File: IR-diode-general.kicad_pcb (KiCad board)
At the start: 2 copper layers, 80 x 20.5 mm, 39 parts, among them J1 BarrelJack_3167288, J2 USB4105-GF-A, U1 QFN10_MP2483DQ_MNP, U2 AP62301Z6-7, U3 SM02B-SRSS-TB-LF-SN, U4 SM02B-SRSS-TB-LF-SN

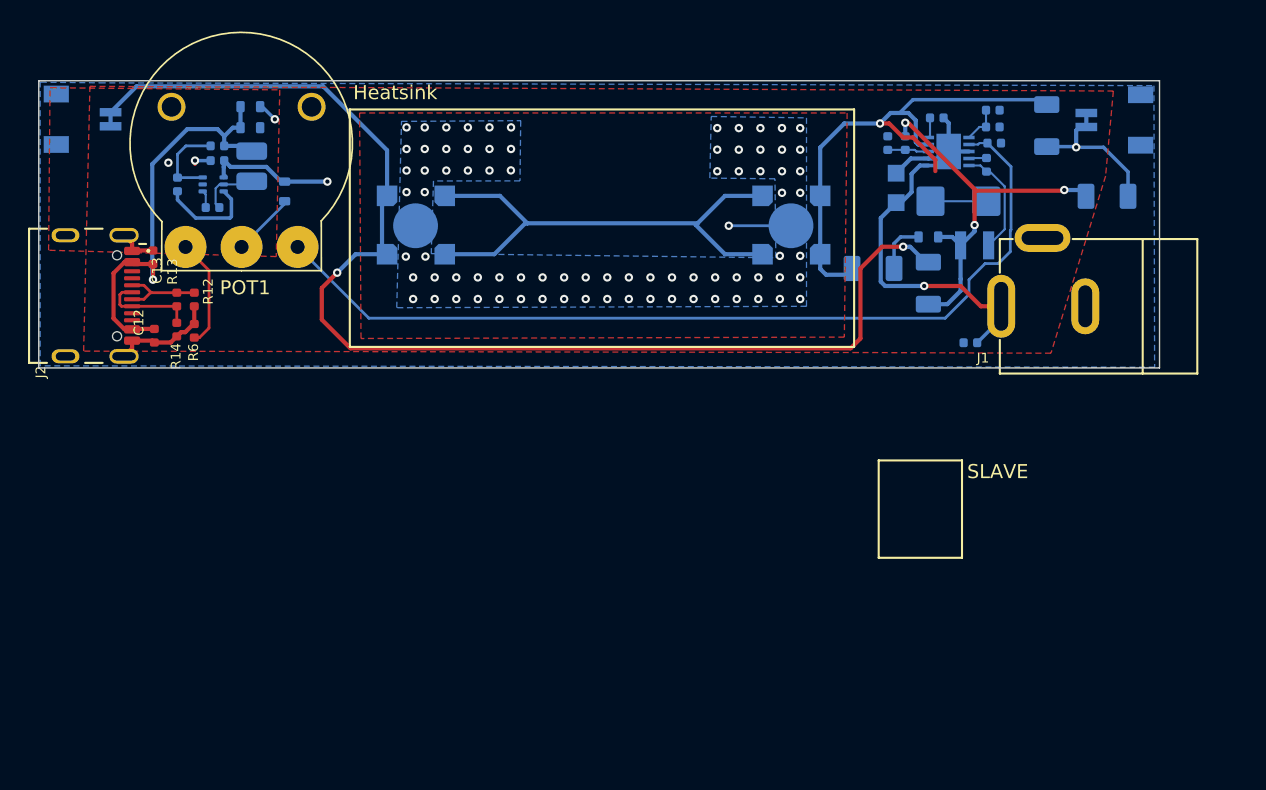
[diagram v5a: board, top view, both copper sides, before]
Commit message: Improving power rail tracks and planes
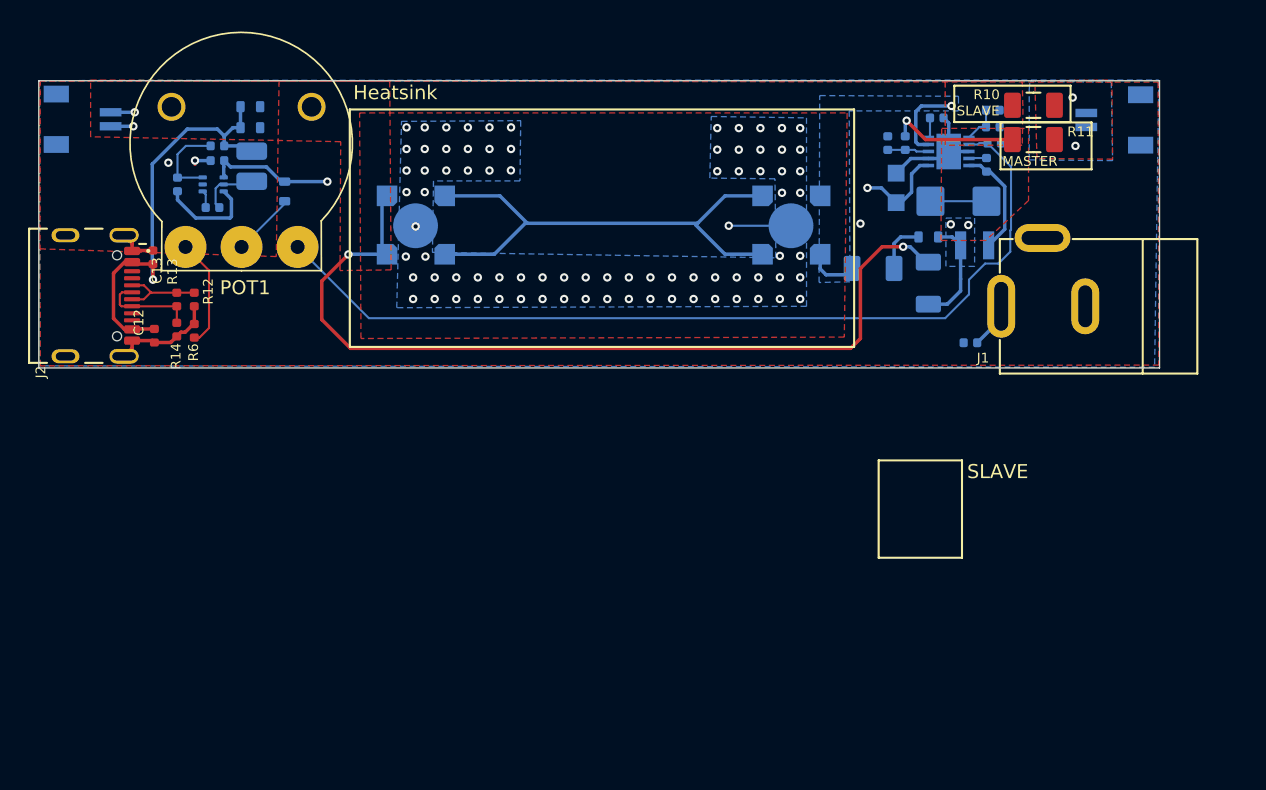
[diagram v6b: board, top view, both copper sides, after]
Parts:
- R10, R11: moved to F.Cu
- moved R11 6.63 mm to (156.0, 44.7)
- moved R10 1.73 mm to (156.0, 42.2), turned to 180 degrees
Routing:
- net FB: track 38.7 -> 9.55 mm
- net A_in: track 89.6 -> 66.6 mm, vias 2 -> 4
- net +12V: track 32.0 -> 19.1 mm
- net SW: track 28.3 -> 17.1 mm
- net C_out: track 11.3 -> 0.90 mm, vias 1 -> 2
- net GND: track 33.0 -> 31.7 mm
- net Thermal: vias 80 -> 81
- added copper zone on F.Cu, net A_in
- added copper zone on B.Cu, net C_out
- added copper zone on F.Cu, net C_out
- added copper zone on B.Cu, net FB
- added copper zone on F.Cu, net FB
- added copper zone on B.Cu, net SW
- added copper zone on F.Cu, net SW
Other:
- board text added: "DBG"

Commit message: Updated design rules
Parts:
- C6: value C_10p_0402 -> C_10u_25V_0603; footprint antmicro-footprints:C_0402_1005Metric -> antmicro-footprints:C_0603_1608Metric
- U1: value QFN10_MP2483DQ_MNP -> MP2483DQ-LF-P
- moved R8 0.55 mm to (97.8, 44.6)
- moved C6 0.43 mm to (97.4, 46.0), turned to 0 degrees
- moved C13 0.30 mm to (93.5, 53.0)
- moved POT1 0.27 mm to (99.6, 44.6)
- turned D1 to 180 degrees
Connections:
- C6 pad 1: +12V -> GND
- C6 pad 2: GND -> +12V
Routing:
- net (no net): track 4.00 -> 0.00 mm
- net FB: track 9.55 -> 5.87 mm
- net +12V: track 19.1 -> 17.0 mm
- net GND: track 31.7 -> 29.9 mm, vias 3 -> 2
- net Net-(C3-Pad1): track 7.86 -> 9.23 mm
- net A_in: track 66.6 -> 65.3 mm
- net /LED DRIVER & USB-C Power output/VBUS: track 31.2 -> 30.3 mm
- net C_out: track 0.90 -> 0.00 mm

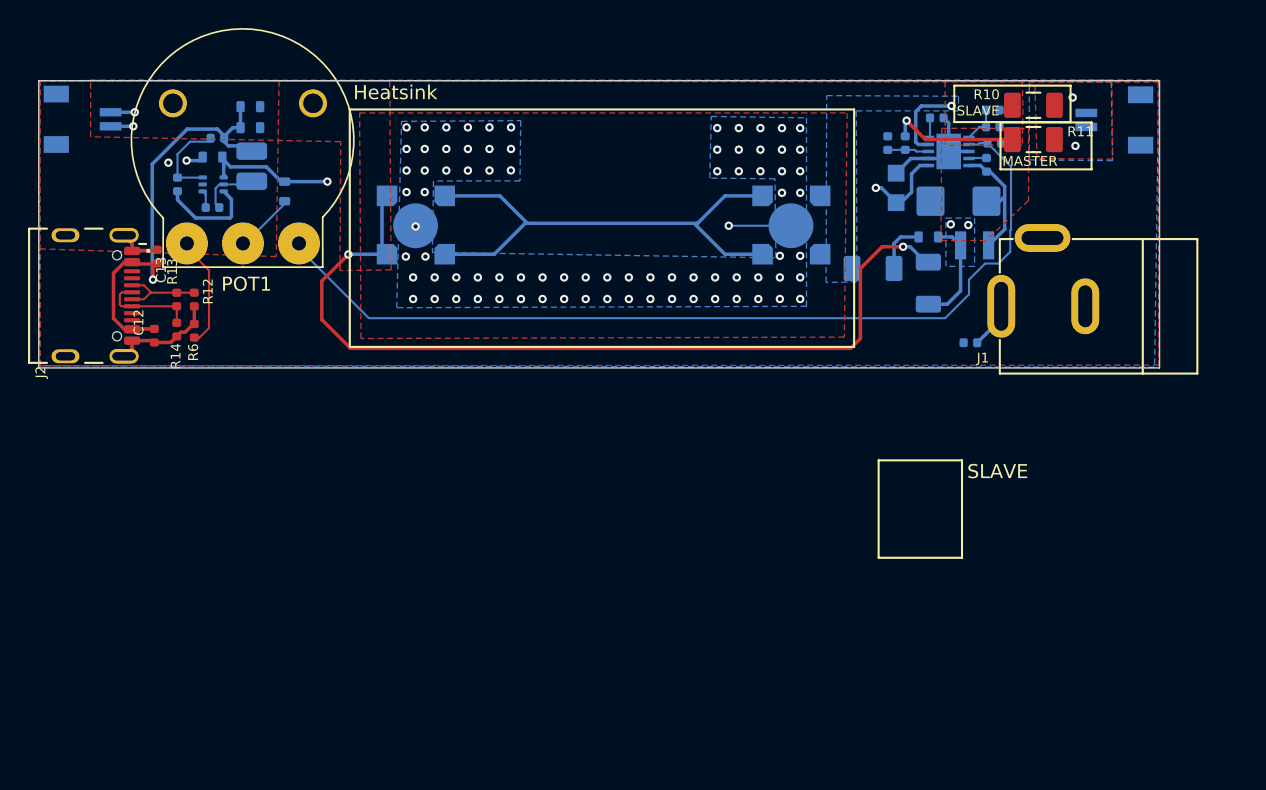
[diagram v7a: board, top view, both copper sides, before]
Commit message: Power rail routing changes
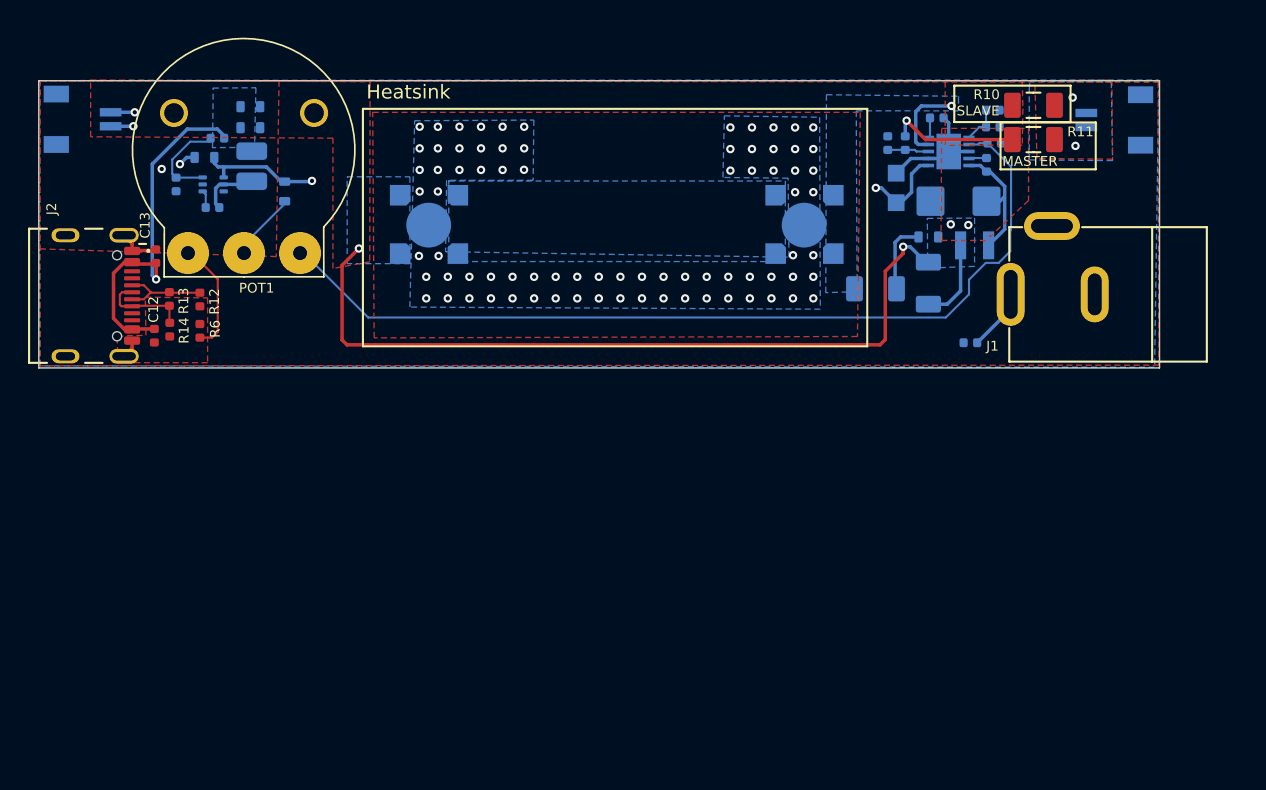
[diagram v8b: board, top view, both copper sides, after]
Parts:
- U1: value MP2483DQ-LF-P -> QFN10_MP2483DQ_MNP
- moved R1 1.46 mm to (144.7, 55.4)
- moved J1 1.09 mm to (154.4, 55.8)
- moved D3 0.94 mm to (139.7, 50.8)
- moved D2 0.94 mm to (112.9, 50.8)
- moved POT1 0.69 mm to (99.7, 45.3)
- moved C6 0.58 mm to (96.8, 46.0)
- moved R13 0.53 mm to (94.3, 56.1)
- moved R14 0.50 mm to (94.3, 58.3)
- moved R12 0.40 mm to (96.5, 56.1)
- moved R6 0.40 mm to (96.5, 58.4)
- moved C13 0.10 mm to (93.3, 53.0)
- moved R9 0.10 mm to (94.8, 47.9)
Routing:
- net Net-(D2-Pad1): track 36.9 -> 0.00 mm
- net GND: track 29.9 -> 18.1 mm
- net A_in: track 65.3 -> 58.7 mm
- net /LED DRIVER & USB-C Power output/VBUS: track 30.3 -> 25.4 mm
- net Thermal: track 4.40 -> 0.00 mm, vias 81 -> 79
- net SW: track 17.1 -> 15.2 mm
- net Net-(POT1-Pad1): track 7.82 -> 8.50 mm
- net Net-(J2-PadA6): track 6.95 -> 6.40 mm
- added copper zone on B.Cu, net /LED DRIVER & USB-C Power output/VBUS
- added copper zone on B.Cu, net A_in
- added copper zone on B.Cu, net Net-(D2-Pad1)
